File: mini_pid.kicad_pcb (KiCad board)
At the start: 2 copper layers, 329.6 x 208.1 mm, 128 parts, among them J1 DB9, P1 Servo In/Ext. Mod, P2 Output/Monitor, P3 Servo In/Ext. Mod, P4 Output/Monitor, U1 ED2610, U2 OPA4227, U3 OPA2227, U4 8DIP, U5 8DIP, U6 OPA4227, U7 OPA2227, U8 8DIP, U9 8DIP

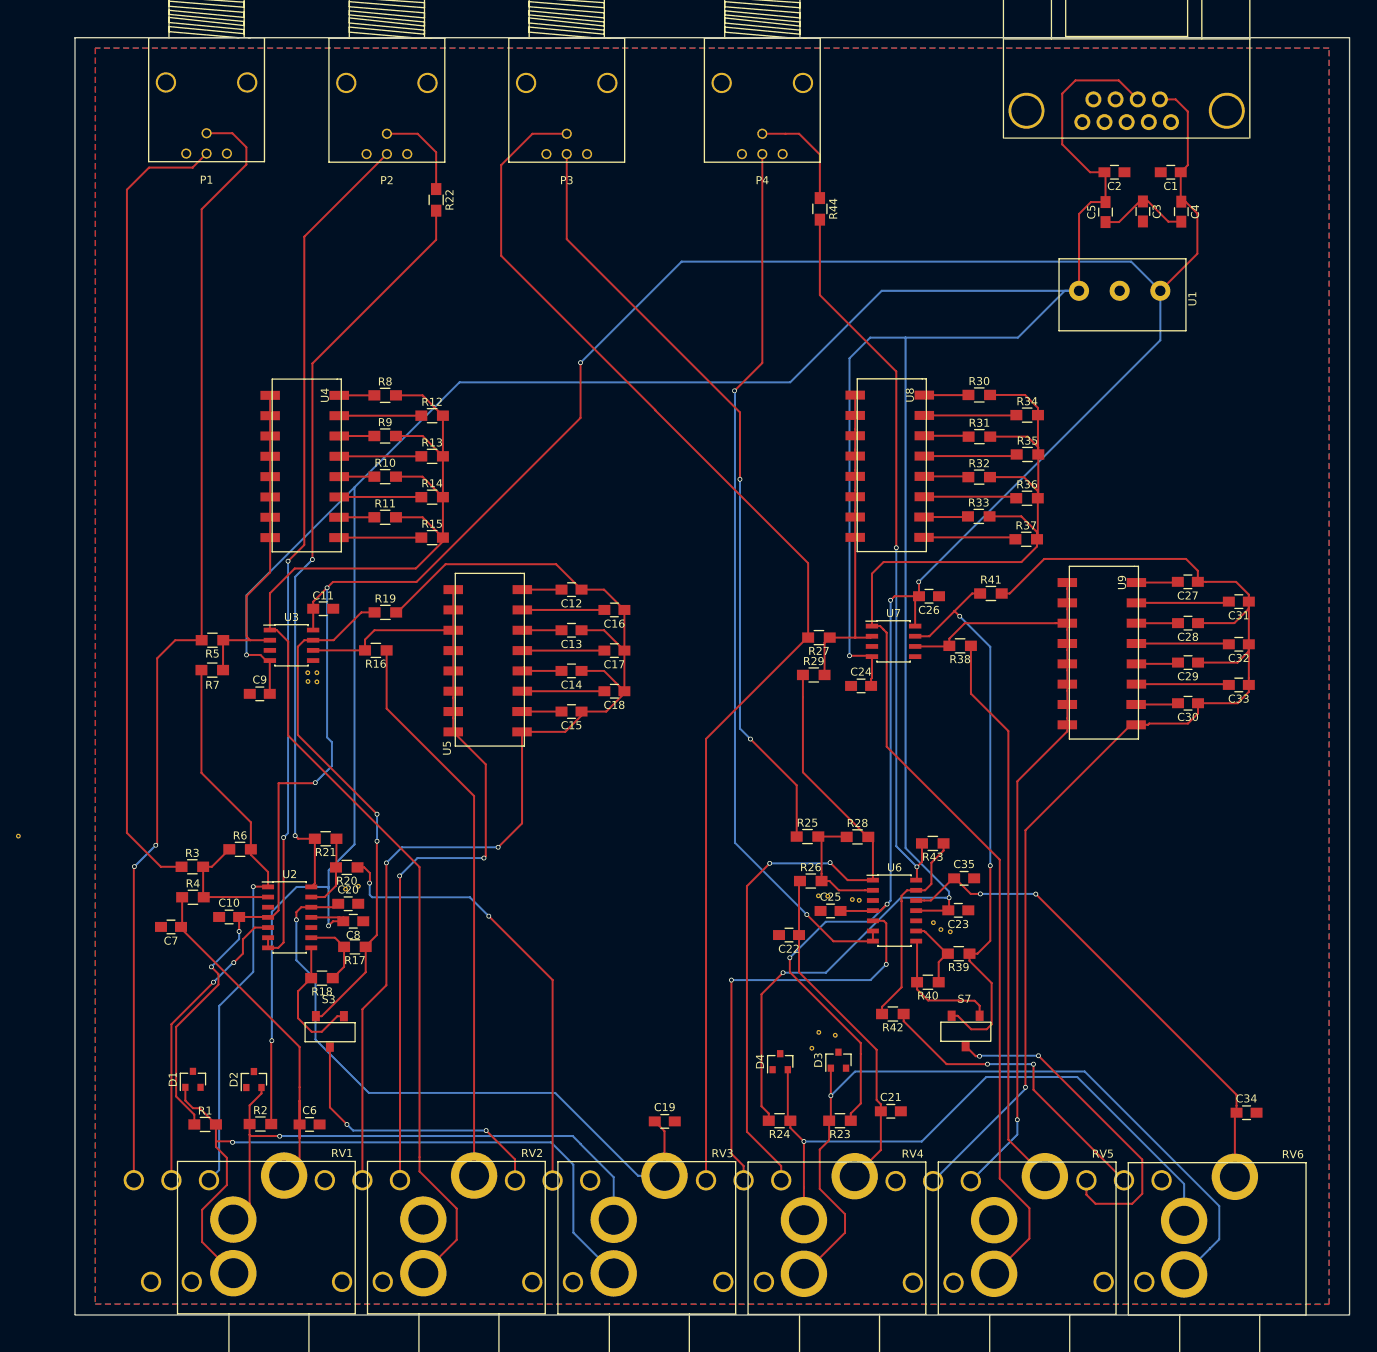
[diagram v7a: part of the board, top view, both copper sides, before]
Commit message: Spaced out components
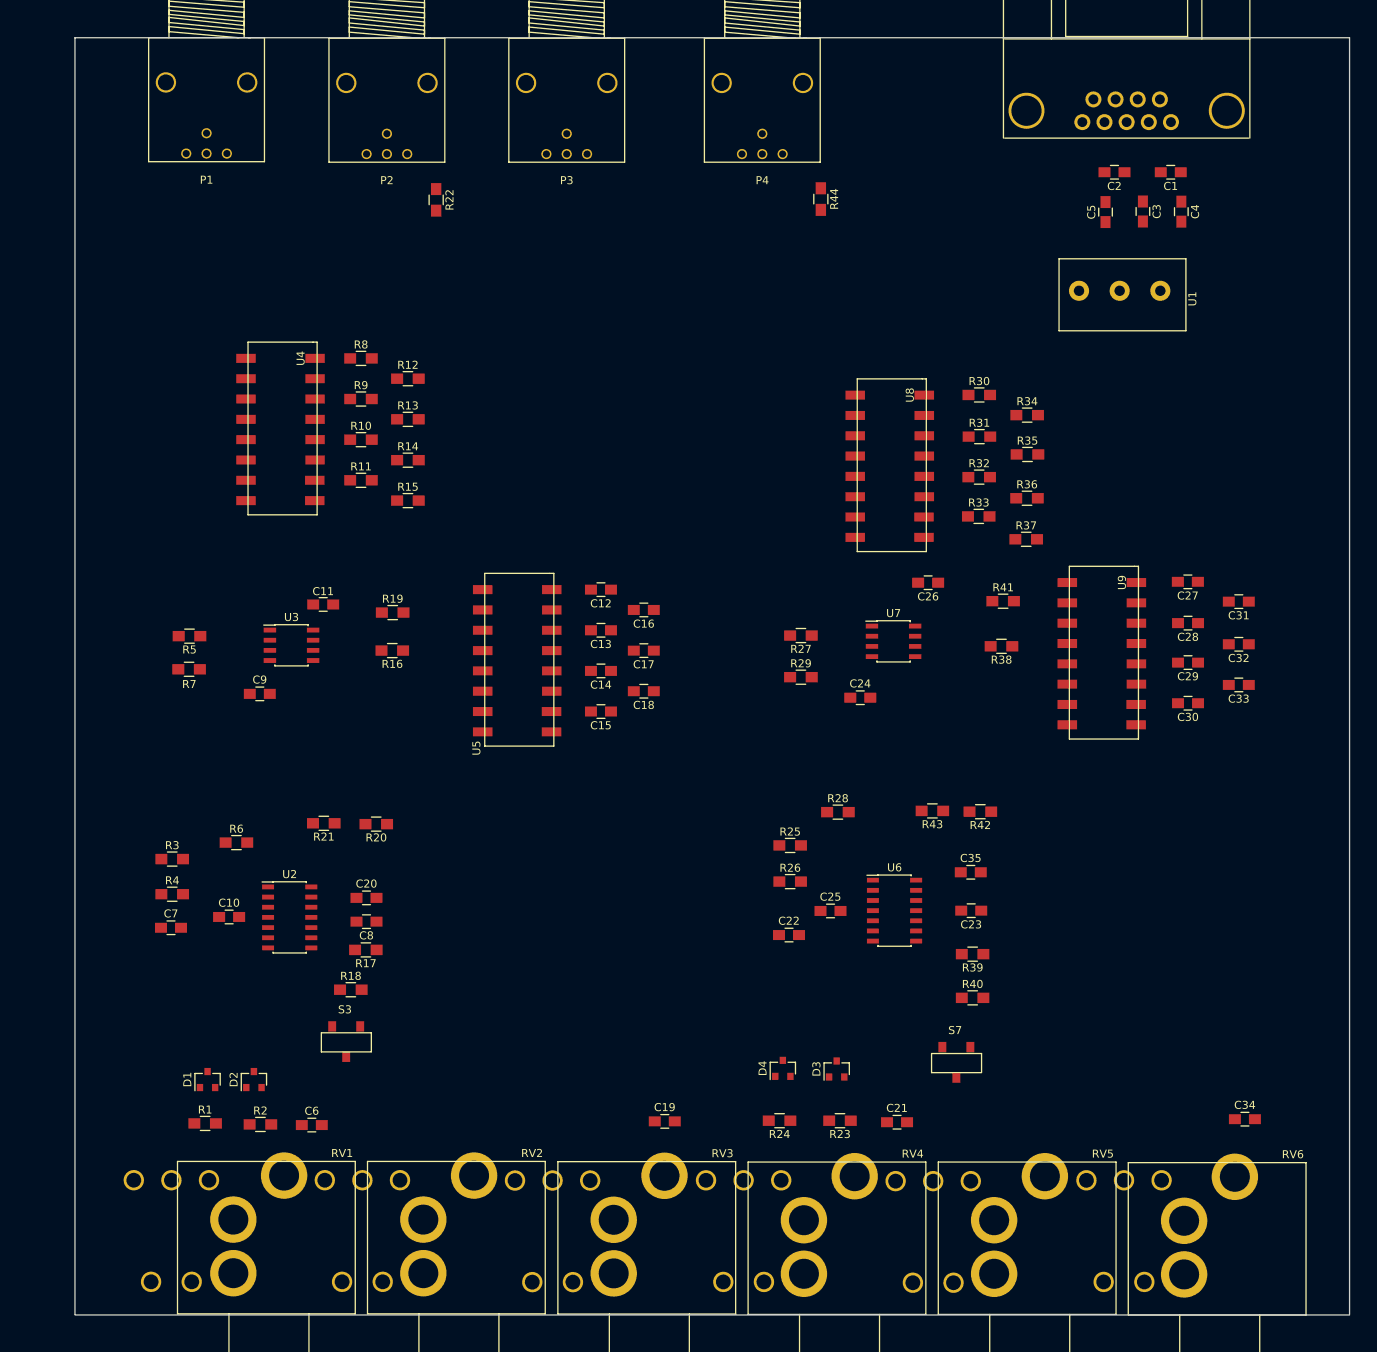
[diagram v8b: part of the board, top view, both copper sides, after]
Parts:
- removed REF** (x17): Via-0.6mm, footprints:Via-0.6mm
- moved R42 27.5 mm to (138.9, 148.9)
- moved R20 6.54 mm to (63.4, 150.5)
- moved R40 5.92 mm to (137.9, 172.2), turned to 0 degrees
- moved R10 5.52 mm to (61.5, 102.4)
- moved R11 5.52 mm to (61.5, 107.5)
- moved R12 5.52 mm to (67.3, 94.8)
- moved R13 5.52 mm to (67.3, 99.9)
- moved R14 5.52 mm to (67.3, 105.0)
- moved R15 5.52 mm to (67.3, 110.1)
- moved R8 5.52 mm to (61.5, 92.3)
- moved R9 5.52 mm to (61.5, 97.4)
- moved U4 5.52 mm to (47.1, 92.3)
- moved R38 5.17 mm to (141.5, 128.3)
- moved S7 4.09 mm to (136.0, 180.6)
- moved R43 4.07 mm to (132.9, 148.8)
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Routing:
- net -15V: track 472.2 -> 0.00 mm, vias 6 -> 0
- net +15V: track 387.0 -> 0.00 mm, vias 9 -> 0
- net Net-(R30-Pad2): track 166.9 -> 0.00 mm
- net Net-(R10-Pad2): track 164.6 -> 0.00 mm
- net Net-(P3-Pad1): track 158.0 -> 0.00 mm
- net Net-(C27-Pad1): track 147.1 -> 0.00 mm, vias 1 -> 0
- net Net-(C12-Pad1): track 143.1 -> 0.00 mm, vias 2 -> 0
- net Net-(P1-Pad1): track 142.6 -> 0.00 mm, vias 2 -> 0
- net Net-(P4-Pad3): track 111.2 -> 0.00 mm, vias 2 -> 0
- net Net-(P2-Pad3): track 107.4 -> 0.00 mm, vias 2 -> 0
- net Net-(R16-Pad2): track 104.2 -> 0.00 mm, vias 2 -> 0
- net Net-(P1-Pad3): track 100.8 -> 0.00 mm
- net Net-(R38-Pad2): track 100.6 -> 0.00 mm, vias 1 -> 0
- net Net-(P3-Pad3): track 97.2 -> 0.00 mm, vias 2 -> 0
- net /PI Circuit 2/+5V: track 96.8 -> 0.00 mm, vias 1 -> 0
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- removed copper zone on B.Cu, net GND
- removed copper zone on F.Cu, net GND
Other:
- net class Power added: clearance 0.4, trace_width 0.5, via_dia 0.6, via_drill 0.4
